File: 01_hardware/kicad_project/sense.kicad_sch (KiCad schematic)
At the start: 22 parts, among them U7 INA181A1IDBVR, U8 INA181A2IDBVR

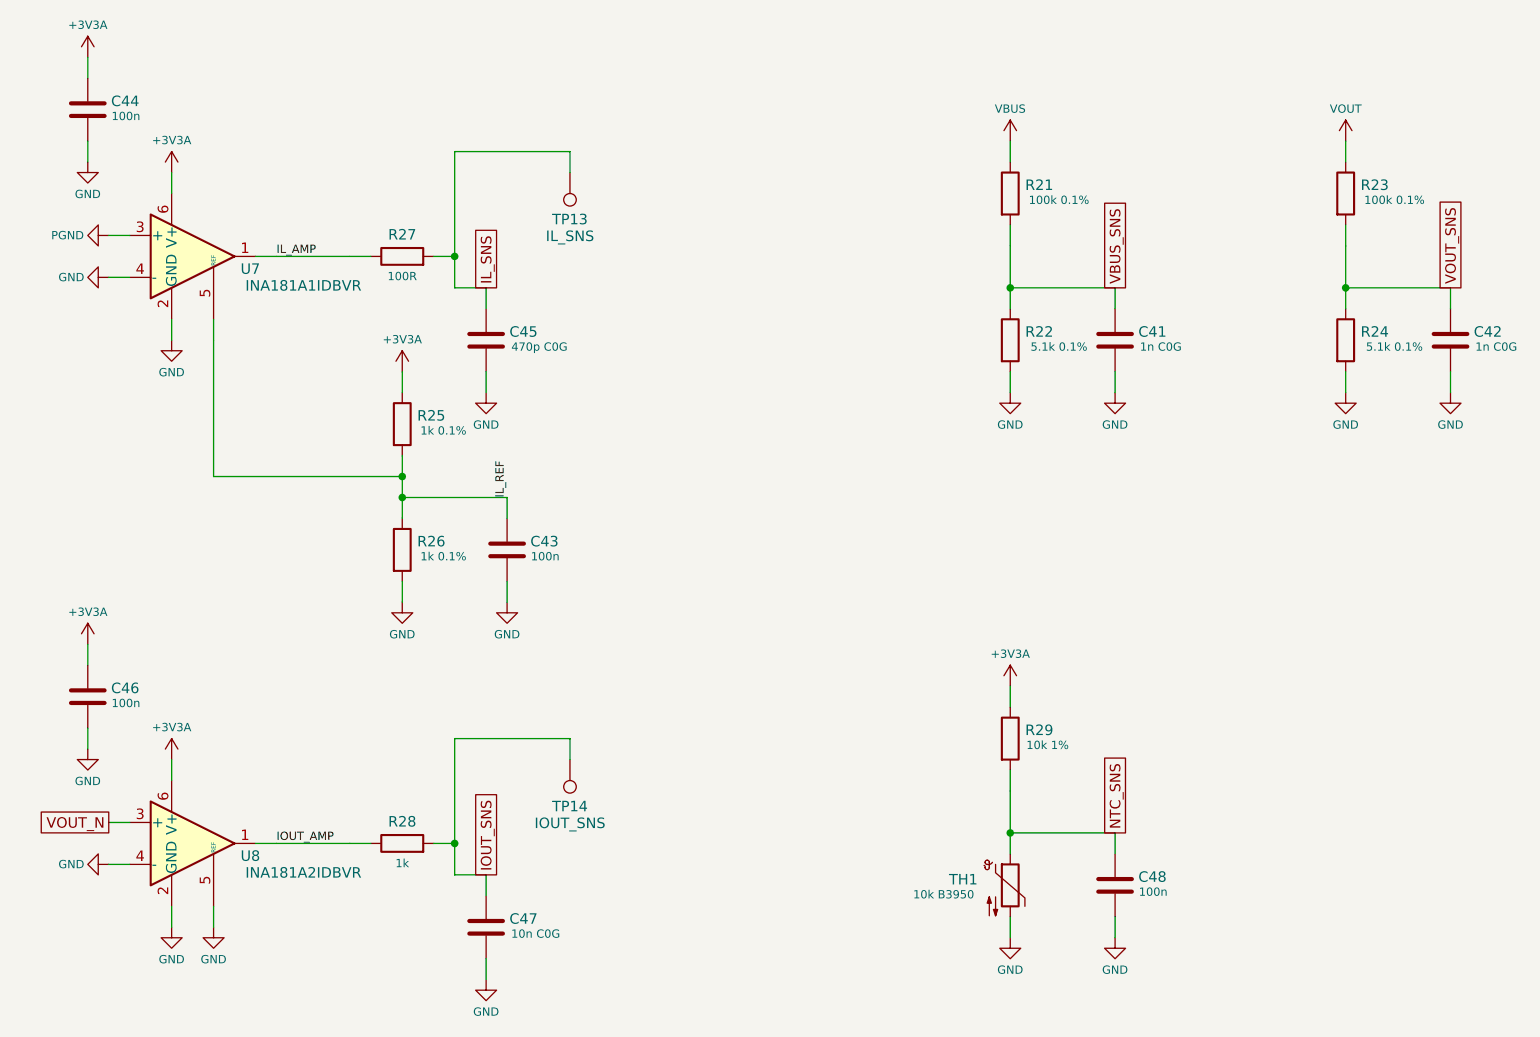
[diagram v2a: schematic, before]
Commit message: External REF3030 ADC reference; full review and documentation update
- U19 REF3030AIDBZR (3.000 V +/-0.2 %, LCSC C38423) + C85 drive VREF+ (new net
  VREF_ADC); VREF+ separated from VDDA; R25 (IL zero) and R29 (NTC pull-up)
  moved to VREF_ADC so those channels are ratiometric
- Full scales: VBUS/VOUT 61.8 V, IL +/-18.75 A, IOUT 6.0 A, DAC/COMP 0-3.0 V
- PCB: U19/C85 placed and routed, pins 28/29 hand-routed; DRC clean, parity
  OK, isolation 4.0 mm
- Design notes (DOCX/PDF), root and firmware READMEs, pin-map, layout review
  image, BOM, Gerbers, CPL, EasyEDA zip and PDFs updated

Co-Authored-By: Claude Opus 5.5 <noreply@anthropic.com>
Claude-Session: https://claude.ai/code/session_01A35wrnwFKLPSaRSxxHs471
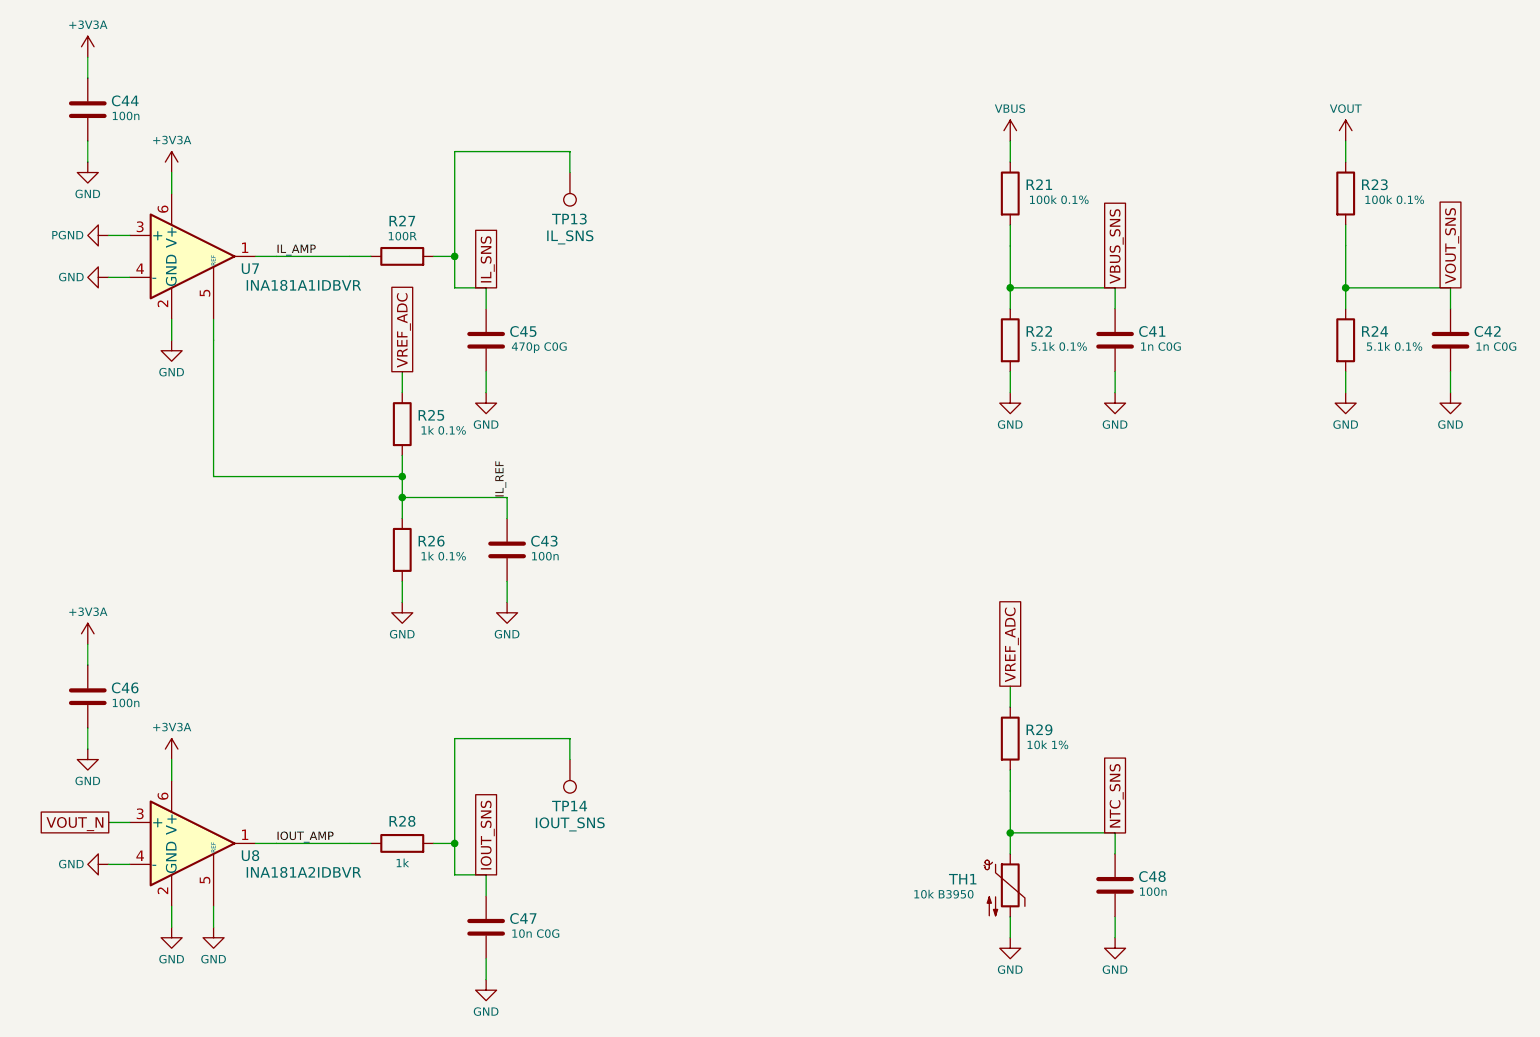
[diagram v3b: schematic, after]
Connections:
- net +3V3A: no longer R25.1, R29.1
- new net VREF_ADC: R25.1, R29.1
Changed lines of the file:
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@@
+    )
+  )
+  (global_label "VREF_ADC" (shape passive) (at 132.08 95.25 90)
+    (effects (font (size 1.27 1.27)) (justify left))
+    (property "Intersheet References" "${INTERSHEET_REFS}" (id 0) (at 132.08 95.25 0)
+      (effects (font (size 1.27 1.27)) hide)
+    )
+  )
+  (global_label "VREF_ADC" (shape passive) (at 205.74 133.35 90)
+    (effects (font (size 1.27 1.27)) (justify left))
+    (property "Intersheet References" "${INTERSHEET_REFS}" (id 0) (at 205.74 133.35 0)
+      (effects (font (size 1.27 1.27)) hide)
     )
   )
@@
     (pin "1")
   )
-  (symbol (lib_id "pwr:+3V3A") (at 132.08 95.25 0) (unit 1)
-    (in_bom no) (on_board yes)
-    (property "Reference" "#PWRSEN022" (id 0) (at 132.08 95.25 0)
-      (effects (font (size 1.27 1.27)) hide)
-    )
-    (property "Value" "+3V3A" (id 1) (at 132.08 91.35 0)
-      (effects (font (size 1.0 1.0)))
-    )
-    (property "Footprint" "" (id 2) (at 132.08 95.25 0)
-      (effects (font (size 1.27 1.27)) hide)
-    )
-    (property "Datasheet" "" (id 3) (at 132.08 95.25 0)
-      (effects (font (size 1.27 1.27)) hide)
-    )
-    (pin "1")
-  )
   (symbol (lib_id "pwr:+3V3A") (at 93.98 57.15 0) (unit 1)
     (in_bom no) (on_board yes)
-    (property "Reference" "#PWRSEN023" (id 0) (at 93.98 57.15 0)
+    (property "Reference" "#PWRSEN022" (id 0) (at 93.98 57.15 0)
       (effects (font (size 1.27 1.27)) hide)
     )
@@
   (symbol (lib_id "pwr:+3V3A") (at 104.14 142.24 0) (unit 1)
     (in_bom no) (on_board yes)
-    (property "Reference" "#PWRSEN024" (id 0) (at 104.14 142.24 0)
+    (property "Reference" "#PWRSEN023" (id 0) (at 104.14 142.24 0)
       (effects (font (size 1.27 1.27)) hide)
     )
@@
   (symbol (lib_id "pwr:+3V3A") (at 93.98 128.27 0) (unit 1)
     (in_bom no) (on_board yes)
-    (property "Reference" "#PWRSEN025" (id 0) (at 93.98 128.27 0)
+    (property "Reference" "#PWRSEN024" (id 0) (at 93.98 128.27 0)
       (effects (font (size 1.27 1.27)) hide)
     )
@@
     )
     (property "Datasheet" "" (id 3) (at 93.98 128.27 0)
-      (effects (font (size 1.27 1.27)) hide)
-    )
-    (pin "1")
-  )
-  (symbol (lib_id "pwr:+3V3A") (at 205.74 133.35 0) (unit 1)
-    (in_bom no) (on_board yes)
-    (property "Reference" "#PWRSEN026" (id 0) (at 205.74 133.35 0)
-      (effects (font (size 1.27 1.27)) hide)
-    )
-    (property "Value" "+3V3A" (id 1) (at 205.74 129.45 0)
-      (effects (font (size 1.0 1.0)))
-    )
-    (property "Footprint" "" (id 2) (at 205.74 133.35 0)
-      (effects (font (size 1.27 1.27)) hide)
-    )
-    (property "Datasheet" "" (id 3) (at 205.74 133.35 0)
       (effects (font (size 1.27 1.27)) hide)
     )
@@
   (symbol (lib_id "Device:R") (at 132.08 81.28 90) (unit 1)
     (in_bom yes) (on_board yes)
-    (property "Reference" "R27" (id 0) (at 132.08 78.648 90)
-      (effects (font (size 1.27 1.27)))
-    )
-    (property "Value" "100R" (id 1) (at 132.08 83.696 90)
-      (effects (font (size 1.0 1.0)))
-    )
+    (property "Reference" "R27" (id 0) (at 132.08 77.048 90)
+      (effects (font (size 1.27 1.27)))
+    )
+    (property "Value" "100R" (id 1) (at 132.08 78.864 90)
+      (effects (font (size 1.0 1.0)))
+    )

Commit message: Rev D order prep: common F1/L2/L3 parts, JLC-checked LCSC numbers, assembly files
- F1: 2512 -> 1206 7 A 63 V fuse (Littelfuse 0458007.DR, C206980; 2nd source Schurter 3413.0326.11)
- L2/L3: SRP5030 -> 5040 shielded 47 uH (SWPA5040S470MT, C86617; 2nd source SRN5040-470M, NRS5040T470MMGK)
- EN_AUX re-routed off the L2 pad gap; VIN track centred between the L3 pads (0.4 mm each side)
- LCSC numbers checked in the JLCPCB library for every assembled part (design.py JLC_LCSC),
  written to the BOMs, schematic and PCB fields
- New JLC assembly upload files DCDC_JLC_BOM.csv / DCDC_JLC_CPL.csv (217 parts; U1, T1,
  connectors, headers and SW1 hand-soldered) and jlc_order_files.py to rebuild them
- 03_calculations/aux_fuse_check.py: aux inductor peak 0.27 A vs 1.1 A Isat; F1 4.8 A at 12 V / 50 W
- Design notes (docx/pdf), README, Gerbers, CPL, PDFs and DRC report regenerated
- Checks: DRC (JLC rules) 0 errors / 0 unconnected, netlist 134 nets / 257 parts 0 errors,
  isolation check 0 errors, silkscreen clean

Co-Authored-By: Claude Opus 5.5 <noreply@anthropic.com>
Claude-Session: https://claude.ai/code/session_01A35wrnwFKLPSaRSxxHs471
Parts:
- C41, C42: LCSC (none) -> C113780
- C43, C44, C46, C48: LCSC (none) -> C1525
- C45: LCSC (none) -> C106259
- C47: LCSC (none) -> C22400107
- R21, R23: LCSC (none) -> C122538
- R22, R24: LCSC (none) -> C186154
- R25, R26: LCSC (none) -> C186137
- R27: LCSC (none) -> C25076
- R28: LCSC (none) -> C11702
- R29: LCSC (none) -> C25744
- TH1: LCSC (none) -> C2892547
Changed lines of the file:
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@@
       (effects (font (size 1.27 1.27)) hide)
     )
-    (property "LCSC" "" (id 4) (at 205.74 73.66 0)
+    (property "LCSC" "C122538" (id 4) (at 205.74 73.66 0)
       (effects (font (size 1.27 1.27)) hide)
     )
@@
       (effects (font (size 1.27 1.27)) hide)
     )
-    (property "LCSC" "" (id 4) (at 205.74 91.44 0)
+    (property "LCSC" "C186154" (id 4) (at 205.74 91.44 0)
       (effects (font (size 1.27 1.27)) hide)
     )
@@
       (effects (font (size 1.27 1.27)) hide)
     )
-    (property "LCSC" "" (id 4) (at 218.44 91.44 0)
+    (property "LCSC" "C113780" (id 4) (at 218.44 91.44 0)
       (effects (font (size 1.27 1.27)) hide)
     )
@@
       (effects (font (size 1.27 1.27)) hide)
     )
-    (property "LCSC" "" (id 4) (at 246.38 73.66 0)
+    (property "LCSC" "C122538" (id 4) (at 246.38 73.66 0)
       (effects (font (size 1.27 1.27)) hide)
     )
@@
       (effects (font (size 1.27 1.27)) hide)
     )
-    (property "LCSC" "" (id 4) (at 246.38 91.44 0)
+    (property "LCSC" "C186154" (id 4) (at 246.38 91.44 0)
       (effects (font (size 1.27 1.27)) hide)
     )
@@
       (effects (font (size 1.27 1.27)) hide)
     )
-    (property "LCSC" "" (id 4) (at 259.08 91.44 0)
+    (property "LCSC" "C113780" (id 4) (at 259.08 91.44 0)
       (effects (font (size 1.27 1.27)) hide)
     )
@@
       (effects (font (size 1.27 1.27)) hide)
     )
-    (property "LCSC" "" (id 4) (at 132.08 101.6 0)
+    (property "LCSC" "C186137" (id 4) (at 132.08 101.6 0)
       (effects (font (size 1.27 1.27)) hide)
     )
@@
       (effects (font (size 1.27 1.27)) hide)
     )
-    (property "LCSC" "" (id 4) (at 132.08 116.84 0)
+    (property "LCSC" "C186137" (id 4) (at 132.08 116.84 0)
       (effects (font (size 1.27 1.27)) hide)
     )
@@
       (effects (font (size 1.27 1.27)) hide)
     )
-    (property "LCSC" "" (id 4) (at 144.78 116.84 0)
+    (property "LCSC" "C1525" (id 4) (at 144.78 116.84 0)
       (effects (font (size 1.27 1.27)) hide)
     )
@@
       (effects (font (size 1.27 1.27)) hide)
     )
-    (property "LCSC" "" (id 4) (at 93.98 63.5 0)
+    (property "LCSC" "C1525" (id 4) (at 93.98 63.5 0)
       (effects (font (size 1.27 1.27)) hide)
     )
@@
       (effects (font (size 1.27 1.27)) hide)
     )
-    (property "LCSC" "" (id 4) (at 132.08 81.28 0)
+    (property "LCSC" "C25076" (id 4) (at 132.08 81.28 0)
       (effects (font (size 1.27 1.27)) hide)
     )
@@
       (effects (font (size 1.27 1.27)) hide)
     )
-    (property "LCSC" "" (id 4) (at 142.24 91.44 0)
+    (property "LCSC" "C106259" (id 4) (at 142.24 91.44 0)
       (effects (font (size 1.27 1.27)) hide)
     )
@@
       (effects (font (size 1.27 1.27)) hide)
     )
-    (property "LCSC" "" (id 4) (at 93.98 134.62 0)
+    (property "LCSC" "C1525" (id 4) (at 93.98 134.62 0)
       (effects (font (size 1.27 1.27)) hide)
     )
@@
       (effects (font (size 1.27 1.27)) hide)
     )
-    (property "LCSC" "" (id 4) (at 132.08 152.4 0)
+    (property "LCSC" "C11702" (id 4) (at 132.08 152.4 0)
       (effects (font (size 1.27 1.27)) hide)
     )
@@
       (effects (font (size 1.27 1.27)) hide)
     )
-    (property "LCSC" "" (id 4) (at 142.24 162.56 0)
+    (property "LCSC" "C22400107" (id 4) (at 142.24 162.56 0)
       (effects (font (size 1.27 1.27)) hide)
     )
@@
       (effects (font (size 1.27 1.27)) hide)
     )
-    (property "LCSC" "" (id 4) (at 205.74 139.7 0)
+    (property "LCSC" "C25744" (id 4) (at 205.74 139.7 0)
       (effects (font (size 1.27 1.27)) hide)
     )
@@
       (effects (font (size 1.27 1.27)) hide)
     )
-    (property "LCSC" "" (id 4) (at 205.74 157.48 0)
+    (property "LCSC" "C2892547" (id 4) (at 205.74 157.48 0)
       (effects (font (size 1.27 1.27)) hide)
     )
@@
       (effects (font (size 1.27 1.27)) hide)
     )
-    (property "LCSC" "" (id 4) (at 218.44 157.48 0)
-      (effects (font (size 1.27 1.27)) hide)
-    )
+    (property "LCSC" "C1525" (id 4) (at 218.44 157.48 0)
+      (effects (font (size 1.27 1.27)) hide)
+    )
